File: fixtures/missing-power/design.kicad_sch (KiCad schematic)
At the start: 0 parts

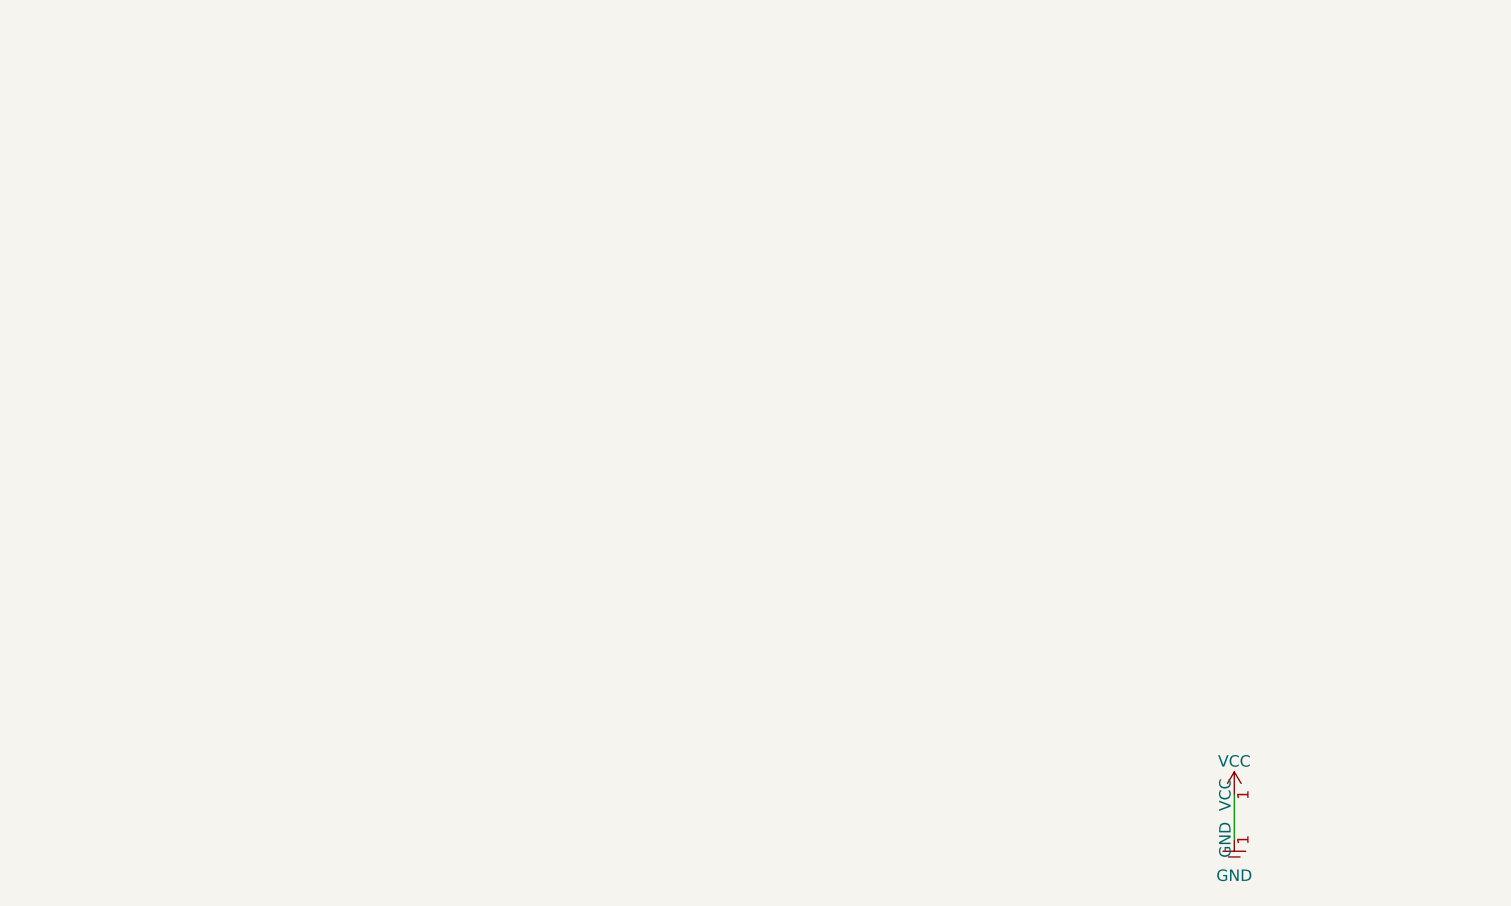
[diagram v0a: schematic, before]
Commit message: fix: missing-power на официальных lib_symbols KiCad 10 — грузится kicad-cli
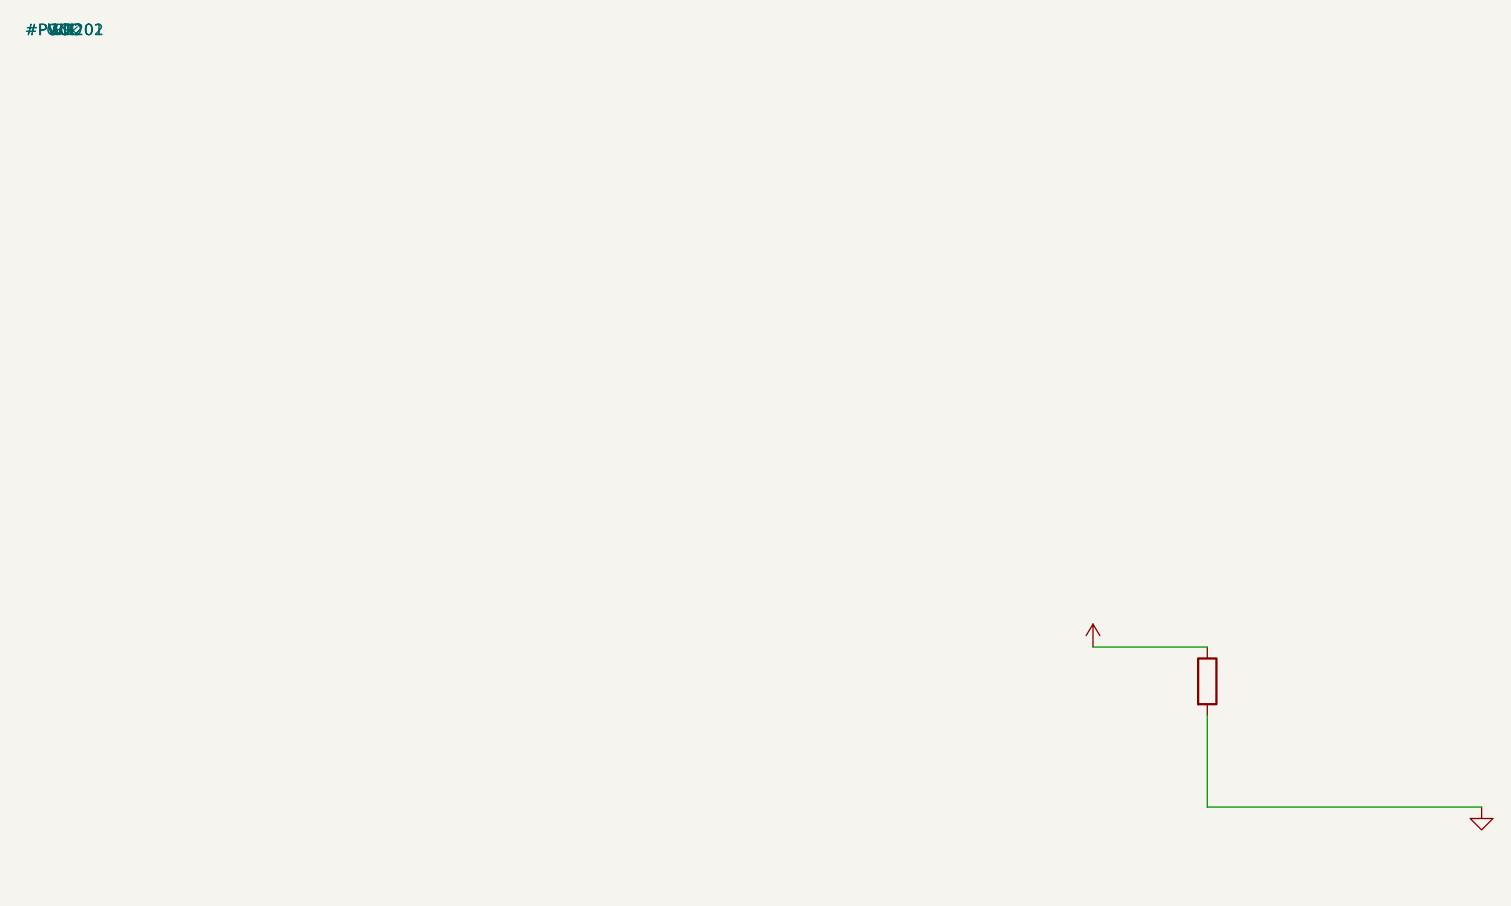
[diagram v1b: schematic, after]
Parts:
- added R1: 10k, symbol Device:R
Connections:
- net GND: now also R1.2
- new net VCC: R1.1
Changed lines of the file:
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@@
     (title "missing-power")
   )
-  (wire (pts (xy 130 85) (xy 130 90)) (stroke (width 0) (type default)))
-  (symbol (lib_id "power:VCC") (at 130 85 0) (unit 1)
-    (property "Reference" "#PWR201" (at 130 88.81 0) (effects (font (size 1.27 1.27)) hide))
-    (property "Value" "VCC" (at 130 81.28 0) (effects (font (size 1.27 1.27))))
-    (pin "1"))
-  (symbol (lib_id "power:GND") (at 130 90 0) (unit 1)
-    (property "Reference" "#PWR202" (at 130 96.35 0) (effects (font (size 1.27 1.27)) hide))
-    (property "Value" "GND" (at 130 93.98 0) (effects (font (size 1.27 1.27))))
-    (pin "1"))
+  (wire (pts (xy 114.3 68.58) (xy 127 68.58)) (stroke (width 0) (type default)))
+  (wire (pts (xy 127 76.2) (xy 127 86.36)) (stroke (width 0) (type default)))
+  (wire (pts (xy 127 86.36) (xy 157.48 86.36)) (stroke (width 0) (type default)))
+  (symbol (lib_id "power:VCC") (at 114.3 68.58 0) (unit 1)
+    (property "Reference" "#PWR201")
+    (property "Value" "VCC")
+    (pin "1")
+  )
+  (symbol (lib_id "Device:R") (at 127 72.39 0) (unit 1)
+    (property "Reference" "R1")
+    (property "Value" "10k")
+    (pin "1")
+    (pin "2")
+  )
+  (symbol (lib_id "power:GND") (at 157.48 86.36 0) (unit 1)
+    (property "Reference" "#PWR202")
+    (property "Value" "GND")
+    (pin "1")
+  )
 )
